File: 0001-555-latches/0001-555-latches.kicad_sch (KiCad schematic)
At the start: 33 parts, among them J1 DC_IN, J2 ASTBL_OUT, J3 MSTBL_OUT, J4 BSTBL_OUT, SW1 SW_Push, SW2 SW_Push, SW3 SW_Push, U1 NE555P, U2 NE555P, U3 NE555P

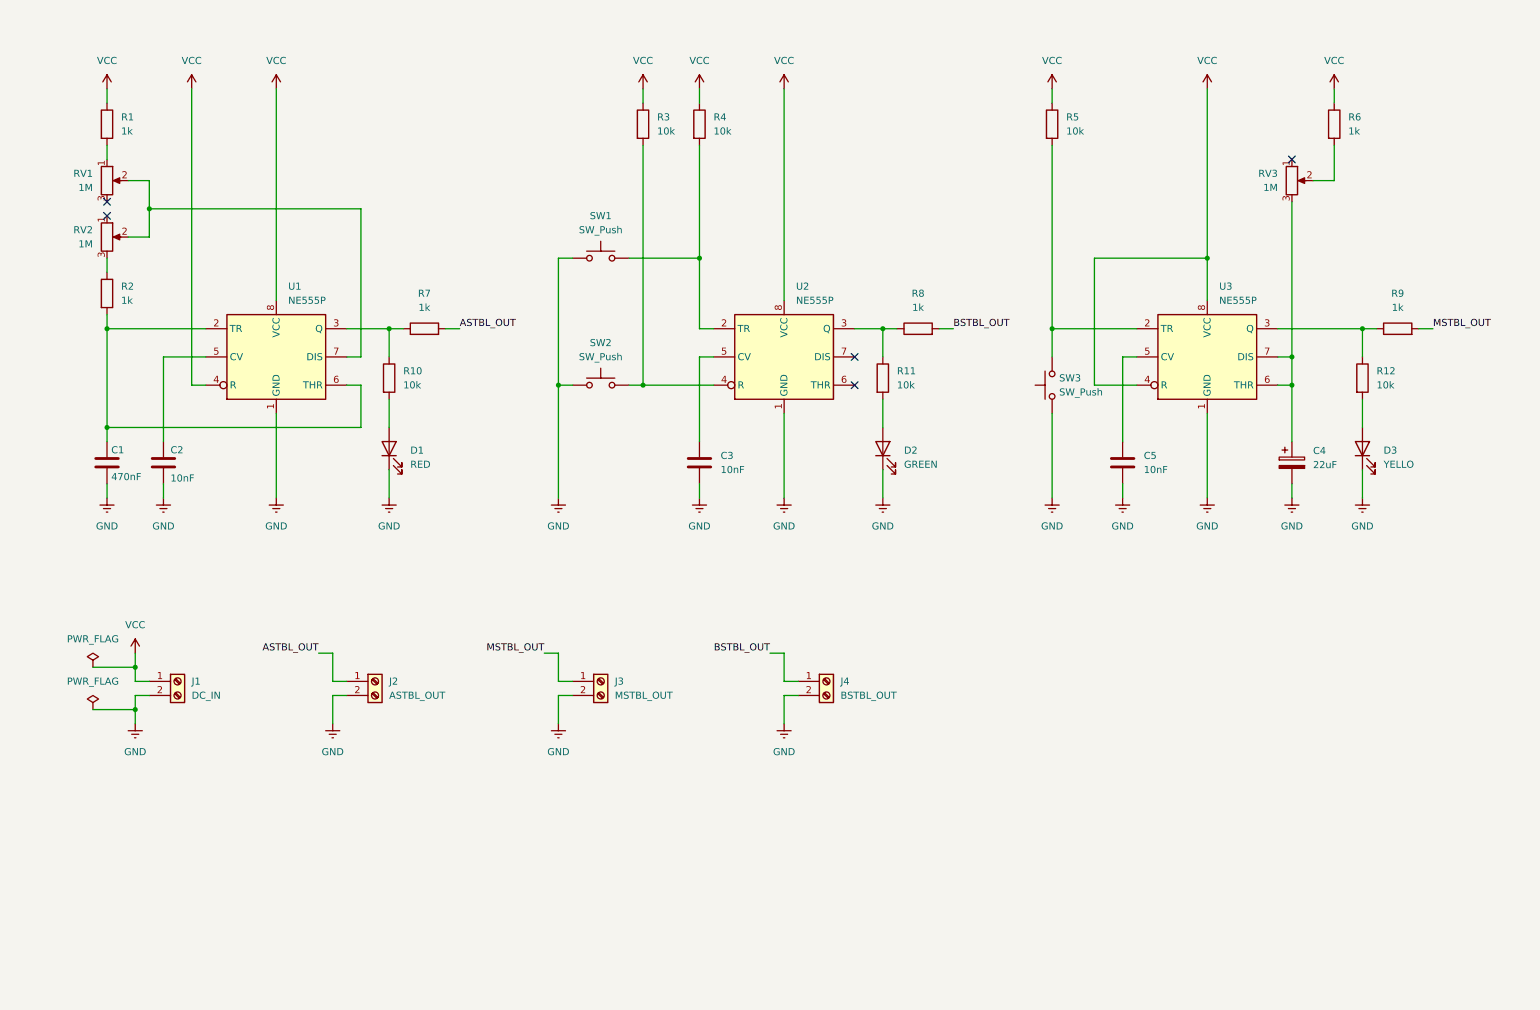
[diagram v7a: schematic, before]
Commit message: Update potentiometers leads, replace junctions
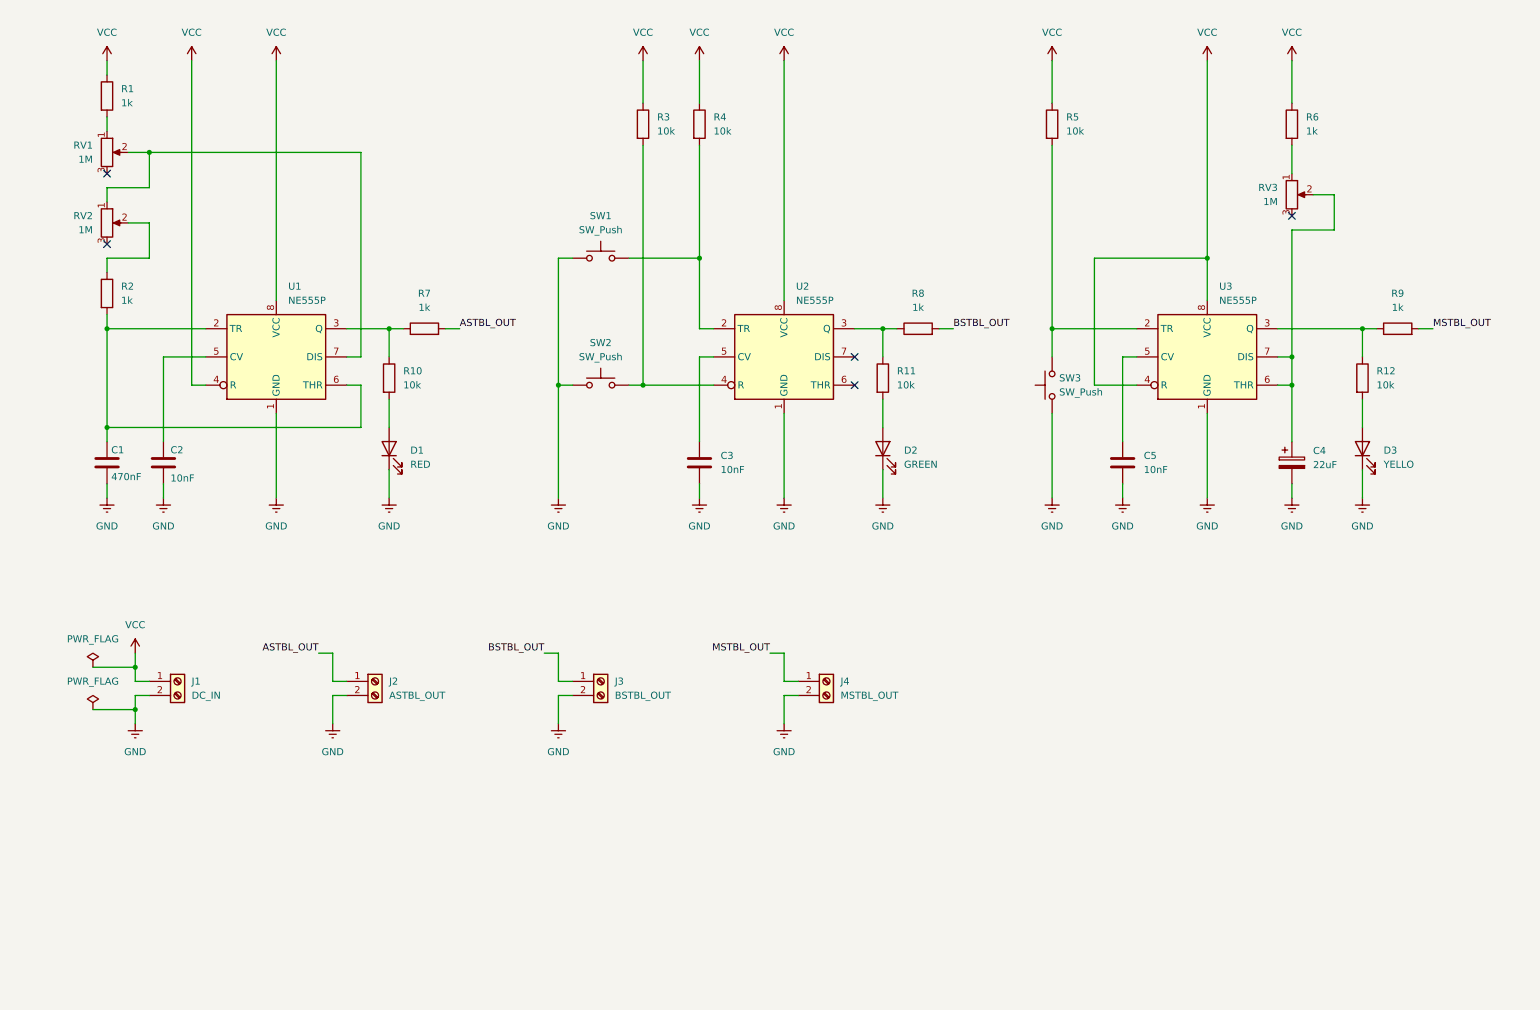
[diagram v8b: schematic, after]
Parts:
- renumbered J4 to J3, J3 to J4
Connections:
- net at RV1.2, U1.7 (DIS): now also RV2.1; no longer RV2.2
- net at R6.2: now also RV3.1; no longer RV3.2
- net at C4.1, U3.6 (THR), U3.7 (DIS): now also RV3.2; no longer RV3.3
- net at R2.1: now also RV2.2; no longer RV2.3
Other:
- moved on the sheet: J3, J4, R1, R6, RV1, RV2, RV3
